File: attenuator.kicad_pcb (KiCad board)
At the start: 2 copper layers, 104.8 x 83.8 mm, 41 parts, among them J1 Conn_01x03_Male, J2 Conn_01x03_Male, J3 Conn_01x02_Male, J4 Conn_01x04_Male, J5 Conn_01x02_Male, K1 G5V-2, K2 G5V-2, K3 G5V-2, K4 G5V-2, K5 G5V-2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

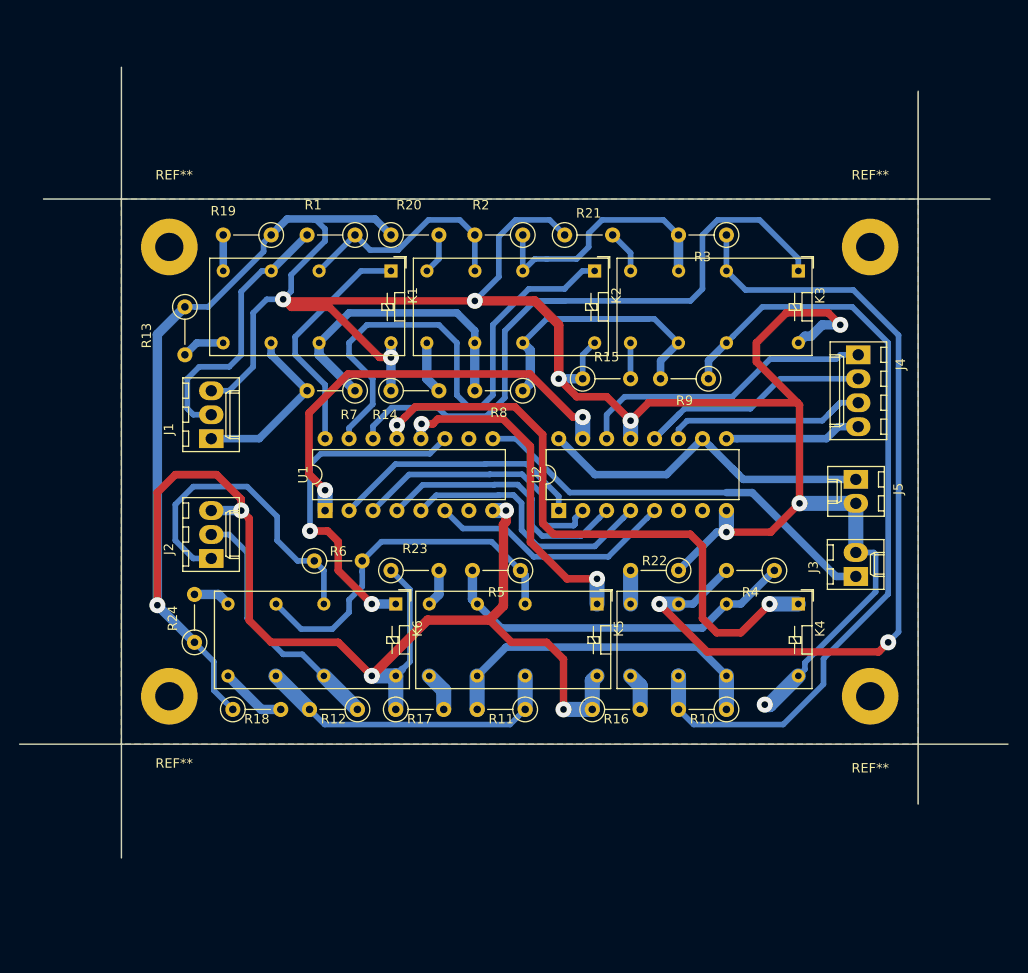
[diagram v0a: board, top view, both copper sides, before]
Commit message: change schema and working on pcb
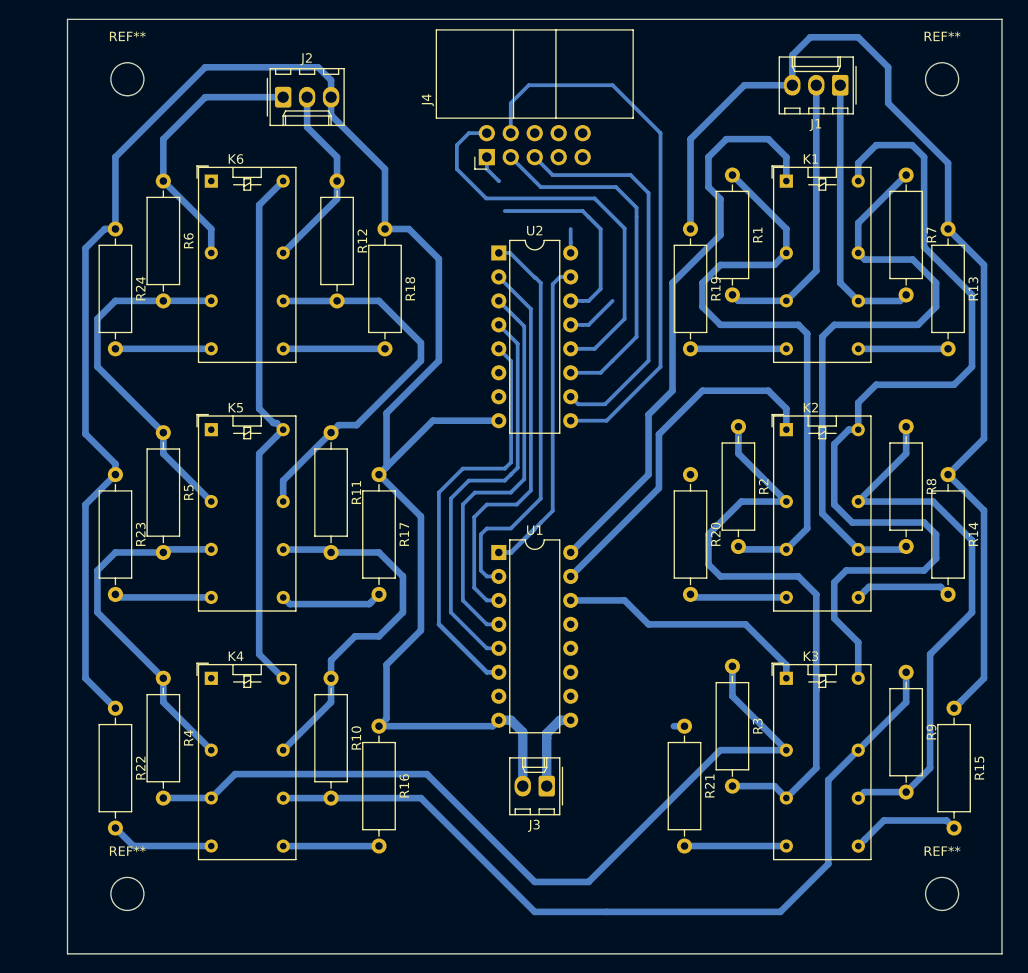
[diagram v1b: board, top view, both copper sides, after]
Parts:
- removed J5: Conn_01x02_Male, Connectors_Molex:Molex_KK-6410-02_02x2.54mm_Straight
- removed the REF** at (90.8, 54.6)
- removed the REF** at (90.8, 102.2)
- removed the REF** at (165.1, 102.2)
- removed the REF** at (165.1, 54.6)
- added REF**: MountingHole_3.5mm, MountingHole:MountingHole_3.5mm, F.Cu at (86.4, 36.8)
- added REF**: MountingHole_3.5mm, MountingHole:MountingHole_3.5mm, F.Cu at (172.7, 36.8)
- added REF**: MountingHole_3.5mm, MountingHole:MountingHole_3.5mm, F.Cu at (172.7, 123.2)
- added REF**: MountingHole_3.5mm, MountingHole:MountingHole_3.5mm, F.Cu at (86.4, 123.2)
- J1, J2: footprint Connectors_Molex:Molex_KK-6410-03_03x2.54mm_Straight -> Connector_Molex:Molex_KK-254_AE-6410-03A_1x03_P2.54mm_Vertical
- J3: footprint Connectors_Molex:Molex_KK-6410-02_02x2.54mm_Straight -> Connector_Molex:Molex_KK-254_AE-6410-02A_1x02_P2.54mm_Vertical
- J4: value Conn_01x04_Male -> Conn_01x05_Male; footprint Connectors_Molex:Molex_KK-6410-04_04x2.54mm_Straight -> Connector_IDC:IDC-Header_2x05_P2.54mm_Horizontal
- K1: footprint Relays_THT:Relay_DPDT_Omron_G5V-2 -> Relay_THT:Relay_DPDT_Omron_G5V-2
- R1, R10, R11, R12, R13, R14, R15, R16, R17, R18, R19, R2, R20, R21, R22, R23, R24, R3, R4, R5, R6, R7, R8, R9: footprint Resistors_THT:R_Axial_DIN0207_L6.3mm_D2.5mm_P5.08mm_Vertical -> Resistor_THT:R_Axial_DIN0309_L9.0mm_D3.2mm_P12.70mm_Horizontal
- U1, U2: footprint Housings_DIP:DIP-16_W7.62mm -> Package_DIP:DIP-16_W7.62mm
- moved R13 81.3 mm to (173.4, 52.7)
- moved J1 76.5 mm to (161.9, 37.5), turned to 180 degrees
- moved R4 65.8 mm to (90.2, 100.3), turned to 270 degrees
- moved R7 62.7 mm to (168.9, 47.0), turned to 270 degrees
- moved K4 62.7 mm to (95.2, 100.3), turned to 0 degrees
- moved R22 61.5 mm to (85.1, 103.5), turned to 270 degrees
- moved R14 59.7 mm to (173.4, 78.7), turned to 270 degrees
- moved R12 56.0 mm to (108.6, 47.6), turned to 270 degrees
- moved R21 53.6 mm to (145.4, 105.4), turned to 270 degrees
- moved R18 53.4 mm to (113.7, 52.7), turned to 270 degrees
- moved R15 52.6 mm to (174.0, 103.5), turned to 270 degrees
- moved J2 49.5 mm to (102.9, 38.7), turned to 0 degrees
- moved K6 48.9 mm to (95.2, 47.6), turned to 0 degrees
- moved R3 45.7 mm to (150.5, 99.1), turned to 270 degrees
- moved K5 44.9 mm to (95.2, 74.0), turned to 0 degrees
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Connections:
- K1 pad 16: GND -> +12V
- K2 pad 16: GND -> +12V
- K3 pad 16: GND -> +12V
- K4 pad 16: GND -> +12V
- K5 pad 16: GND -> +12V
- K6 pad 16: GND -> +12V
- U2 pad 10: +5V -> Net-(J4-Pad5)
- U2 pad 16: +5V -> Net-(J4-Pad5)
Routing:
- net +12V: track 45.0 -> 164.1 mm
- net GND: track 422.2 -> 332.1 mm, vias 14 -> 0
- net /K4: track 65.9 -> 0.00 mm, vias 2 -> 0
- net Net-(J4-Pad5): track 0.00 -> 44.5 mm
- net Net-(J4-Pad4): track 14.5 -> 58.6 mm
- net /K3: track 69.7 -> 27.1 mm
- net Net-(K1-Pad4): track 24.6 -> 64.6 mm
- net Net-(K2-Pad4): track 27.9 -> 65.4 mm
- net +5V: track 37.3 -> 0.00 mm
- net /K6: track 37.1 -> 0.00 mm, vias 2 -> 0
- net /K1: track 25.2 -> 61.4 mm
- net /K5: track 36.0 -> 0.00 mm, vias 2 -> 0
- net Net-(K1-Pad13): track 31.6 -> 65.2 mm
- net Net-(K2-Pad13): track 38.5 -> 58.7 mm
- net /K2: track 56.2 -> 37.4 mm
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- removed copper zone on B.Cu, net GND
- removed copper zone on F.Cu, net GND
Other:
- board size 104.8 x 83.8 mm -> 99.1 x 99.1 mm
- net class Default: clearance 0.5 -> 0.4; trace_width 0.8 -> 0.4; via_dia 1.7 -> 0.8; via_drill 0.7 -> 0.4
- rule pad_to_mask_clearance: 0.2 -> 0
- rule trace_clearance: 0.5 -> 0.4
- rule via_min_drill: 0.7 -> 0.3
- rule via_min_size: 1 -> 0.4

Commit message: Update pcb board
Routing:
- net /K5: track 0.00 -> 8.57 mm, vias 0 -> 2
- net GND: track 332.1 -> 340.5 mm, vias 0 -> 6
- net /K6: track 0.00 -> 8.25 mm, vias 0 -> 2
- net /K4: track 0.00 -> 8.25 mm, vias 0 -> 2
- net +12V: track 164.1 -> 168.6 mm, vias 0 -> 2
- net Net-(J4-Pad1): track 24.1 -> 24.5 mm, vias 0 -> 2
- net Net-(J4-Pad5): vias 0 -> 2
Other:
- net class Default: via_dia 0.8 -> 1.4; via_drill 0.4 -> 0.8
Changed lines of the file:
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@@
     (thickness 1.6)
     (drawings 4)
-    (tracks 367)
+    (tracks 413)
     (zones 0)
     (modules 40)
@@
   )
   (setup
-    (last_trace_width 0.7)
+    (last_trace_width 1)
     (user_trace_width 0.7)
     (user_trace_width 1)
@@
     (segment_width 0.2)
     (edge_width 0.1)
-    (via_size 0.8)
-    (via_drill 0.4)
+    (via_size 1.4)
+    (via_drill 0.8)
     (via_min_size 0.4)
     (via_min_drill 0.3)
@@
     (pad_drill 0.6)
     (pad_to_mask_clearance 0)
+    (solder_mask_min_width 0.25)
     (aux_axis_origin 0 0)
-    (visible_elements FFFFFF7F)
+    (visible_elements 7FFFFFFF)
     (pcbplotparams
       (layerselection 0x010fc_ffffffff)
@@
     (clearance 0.4)
     (trace_width 0.4)
-    (via_dia 0.8)
-    (via_drill 0.4)
+    (via_dia 1.4)
+    (via_drill 0.8)
     (uvia_dia 0.3)
     (uvia_drill 0.1)
@@
   (segment (start 125.095 105.41) (end 125.73 104.775) (width 0.7) (layer B.Cu) (net 3))
   (segment (start 113.03 105.41) (end 125.095 105.41) (width 0.7) (layer B.Cu) (net 3))
-  (segment (start 133.35 62.865) (end 134.62 62.865) (width 0.4) (layer B.Cu) (net 3))
-  (segment (start 134.62 62.865) (end 135.255 62.865) (width 0.4) (layer B.Cu) (net 3))
-  (segment (start 135.255 62.865) (end 137.795 60.325) (width 0.4) (layer B.Cu) (net 3))
   (segment (start 118.745 73.025) (end 113.03 78.74) (width 0.7) (layer B.Cu) (net 3))
-  (segment (start 125.73 73.025) (end 118.745 73.025) (width 0.7) (layer B.Cu) (net 3))
+  (segment (start 125.73 73.025) (end 121.92 73.025) (width 0.7) (layer B.Cu) (net 3))
   (segment (start 113.829999 104.610001) (end 113.829999 98.895001) (width 0.7) (layer B.Cu) (net 3))
   (segment (start 113.03 105.41) (end 113.829999 104.610001) (width 0.7) (layer B.Cu) (net 3))
@@
   (segment (start 117.475 83.185) (end 113.03 78.74) (width 0.7) (layer B.Cu) (net 3))
   (segment (start 117.475 95.25) (end 117.475 83.185) (width 0.7) (layer B.Cu) (net 3))
+  (segment (start 137.795 60.325) (end 137.795 60.325) (width 0.4) (layer B.Cu) (net 3))
+  (via (at 137.795 60.325) (size 1.4) (drill 0.8) (layers F.Cu B.Cu) (net 3))
+  (segment (start 146.05 78.74) (end 146.05 75.565) (width 1) (layer B.Cu) (net 3))
+  (segment (start 146.05 75.565) (end 146.05 75.565) (width 1) (layer B.Cu) (net 3))
+  (via (at 146.05 75.565) (size 1.4) (drill 0.8) (layers F.Cu B.Cu) (net 3))
+  (via (at 135.89 62.23) (size 1.4) (drill 0.8) (layers F.Cu B.Cu) (net 3))
+  (segment (start 135.255 62.865) (end 135.89 62.23) (width 1) (layer B.Cu) (net 3))
+  (segment (start 133.35 62.865) (end 135.255 62.865) (width 1) (layer B.Cu) (net 3))
+  (segment (start 137.795 60.325) (end 135.89 62.23) (width 1) (layer B.Cu) (net 3))
+  (segment (start 145.250001 53.504999) (end 145.250001 54.774999) (width 1) (layer B.Cu) (net 3))
+  (segment (start 146.05 52.705) (end 145.250001 53.504999) (width 1) (layer B.Cu) (net 3))
+  (segment (start 145.250001 54.774999) (end 145.250001 54.774999) (width 1) (layer B.Cu) (net 3))
+  (via (at 145.250001 54.774999) (size 1.4) (drill 0.8) (layers F.Cu B.Cu) (net 3))
+  (segment (start 121.92 73.025) (end 118.745 73.025) (width 0.7) (layer B.Cu) (net 3))
+  (via (at 121.92 73.025) (size 1.4) (drill 0.8) (layers F.Cu B.Cu) (net 3))
+  (segment (start 146.749999 74.865001) (end 147.32 73.025) (width 1) (layer B.Cu) (net 3))
+  (segment (start 146.05 75.565) (end 146.749999 74.865001) (width 1) (layer B.Cu) (net 3))
+  (via (at 147.32 73.025) (size 1.4) (drill 0.8) (layers F.Cu B.Cu) (net 3))
   (segment (start 108.585 49.53) (end 108.585 47.625) (width 0.7) (layer B.Cu) (net 4))
   (segment (start 102.87 55.245) (end 108.585 49.53) (width 0.7) (layer B.Cu) (net 4))
@@
   (segment (start 169.545 43.815) (end 165.735 43.815) (width 0.7) (layer B.Cu) (net 6))
   (segment (start 163.83 45.72) (end 163.83 47.625) (width 0.7) (layer B.Cu) (net 6))
-  (segment (start 163.83 100.33) (end 163.83 96.52) (width 0.7) (layer B.Cu) (net 6))
+  (segment (start 163.83 100.33) (end 163.83 97.155) (width 0.7) (layer B.Cu) (net 6))
   (segment (start 163.83 96.52) (end 161.29 93.98) (width 0.7) (layer B.Cu) (net 6))
   (segment (start 161.29 93.98) (end 161.29 90.17) (width 0.7) (layer B.Cu) (net 6))
@@
   (segment (start 100.33 71.755) (end 100.33 50.165) (width 0.7) (layer B.Cu) (net 6))
   (segment (start 100.33 50.165) (end 102.87 47.625) (width 0.7) (layer B.Cu) (net 6))
+  (segment (start 133.35 104.775) (end 137.795 104.775) (width 1) (layer B.Cu) (net 6))
+  (segment (start 137.795 104.775) (end 137.795 104.775) (width 1) (layer B.Cu) (net 6))
+  (via (at 137.795 104.775) (size 1.4) (drill 0.8) (layers F.Cu B.Cu) (net 6))
+  (segment (start 163.83 97.155) (end 163.83 96.52) (width 0.7) (layer B.Cu) (net 6))
+  (via (at 163.83 97.155) (size 1.4) (drill 0.8) (layers F.Cu B.Cu) (net 6))
   (segment (start 133.35 60.325) (end 134.62 60.325) (width 0.4) (layer B.Cu) (net 7))
   (segment (start 134.62 60.325) (end 135.255 60.325) (width 0.4) (layer B.Cu) (net 7))
   (segment (start 135.255 60.325) (end 136.525 59.055) (width 0.4) (layer B.Cu) (net 7))
   (segment (start 136.525 59.055) (end 136.525 52.705) (width 0.4) (layer B.Cu) (net 7))
-  (segment (start 124.46 46.3486) (end 125.73 47.6186) (width 0.4) (layer B.Cu) (net 7))
+  (segment (start 124.46 46.3486) (end 126.3586 47.6186) (width 0.4) (layer B.Cu) (net 7))
   (segment (start 124.46 45.085) (end 124.46 46.3486) (width 0.4) (layer B.Cu) (net 7))
-  (segment (start 125.73 47.6186) (end 125.73 47.625) (width 0.4) (layer B.Cu) (net 7))
   (segment (start 136.525 52.705) (end 135.255 51.435) (width 0.4) (layer B.Cu) (net 7))
   (segment (start 135.255 51.435) (end 134.62 50.8) (width 0.4) (layer B.Cu) (net 7))
   (segment (start 134.62 50.8) (end 126.365 50.8) (width 0.4) (layer B.Cu) (net 7))
+  (segment (start 126.365 50.8) (end 126.365 50.8) (width 0.4) (layer B.Cu) (net 7))
+  (via (at 126.365 50.8) (size 1.4) (drill 0.8) (layers F.Cu B.Cu) (net 7))
+  (via (at 126.3586 47.6186) (size 1.4) (drill 0.8) (layers F.Cu B.Cu) (net 7))
   (segment (start 122.555 42.545) (end 124.46 42.545) (width 0.4) (layer B.Cu) (net 8))
   (segment (start 121.285 43.815) (end 122.555 42.545) (width 0.4) (layer B.Cu) (net 8))
@@
   (segment (start 133.35 70.485) (end 134.149999 71.284999) (width 0.4) (layer B.Cu) (net 11))
   (segment (start 136.995001 71.284999) (end 141.605 66.675) (width 0.4) (layer B.Cu) (net 11))
-  (segment (start 141.605 66.675) (end 141.605 48.895) (width 0.4) (layer B.Cu) (net 11))
+  (segment (start 141.605 66.675) (end 141.605 52.705) (width 0.4) (layer B.Cu) (net 11))
   (segment (start 134.149999 71.284999) (end 136.995001 71.284999) (width 0.4) (layer B.Cu) (net 11))
   (segment (start 141.605 48.895) (end 139.7 46.99) (width 0.4) (layer B.Cu) (net 11))
@@
   (segment (start 133.35 55.245) (end 133.35 54.11363) (width 0.4) (layer B.Cu) (net 11))
   (segment (start 133.35 54.11363) (end 133.35 52.705) (width 0.4) (layer B.Cu) (net 11))
+  (segment (start 133.35 52.705) (end 133.35 52.705) (width 0.4) (layer B.Cu) (net 11))
+  (via (at 133.35 52.705) (size 1.4) (drill 0.8) (layers F.Cu B.Cu) (net 11))
+  (segment (start 141.605 52.705) (end 141.605 48.895) (width 0.4) (layer B.Cu) (net 11))
+  (via (at 141.605 52.705) (size 1.4) (drill 0.8) (layers F.Cu B.Cu) (net 11))
   (segment (start 163.83 52.07) (end 168.91 46.99) (width 0.7) (layer B.Cu) (net 12))
   (segment (start 163.83 55.245) (end 163.83 52.07) (width 0.7) (layer B.Cu) (net 12))
@@
   (segment (start 86.995 118.11) (end 85.09 116.205) (width 0.7) (layer B.Cu) (net 30))
   (segment (start 95.25 118.11) (end 86.995 118.11) (width 0.7) (layer B.Cu) (net 30))
+  (segment (start 133.35 94.615) (end 137.795 94.615) (width 1) (layer B.Cu) (net 31))
+  (segment (start 137.795 94.615) (end 137.795 94.615) (width 1) (layer B.Cu) (net 31))
+  (via (at 137.795 94.615) (size 1.4) (drill 0.8) (layers F.Cu B.Cu) (net 31))
+  (segment (start 95.25 100.33) (end 95.25 98.63) (width 1) (layer B.Cu) (net 31))
+  (segment (start 95.25 98.63) (end 95.25 96.52) (width 1) (layer B.Cu) (net 31))
+  (segment (start 95.25 96.52) (end 95.25 96.52) (width 1) (layer B.Cu) (net 31))
+  (via (at 95.25 96.52) (size 1.4) (drill 0.8) (layers F.Cu B.Cu) (net 31))
+  (segment (start 133.35 97.155) (end 137.795 97.155) (width 1) (layer B.Cu) (net 32))
+  (segment (start 137.795 97.155) (end 137.795 97.155) (width 1) (layer B.Cu) (net 32))
+  (via (at 137.795 97.155) (size 1.4) (drill 0.8) (layers F.Cu B.Cu) (net 32))
+  (segment (start 95.25 73.9775) (end 95.25 72.2775) (width 1) (layer B.Cu) (net 32))
+  (segment (start 95.25 72.2775) (end 95.25 69.85) (width 1) (layer B.Cu) (net 32))
+  (segment (start 95.25 69.85) (end 95.25 69.85) (width 1) (layer B.Cu) (net 32))
+  (via (at 95.25 69.85) (size 1.4) (drill 0.8) (layers F.Cu B.Cu) (net 32))
   (segment (start 85.4075 91.7575) (end 85.09 91.44) (width 0.7) (layer B.Cu) (net 33))
   (segment (start 95.25 91.7575) (end 85.4075 91.7575) (width 0.7) (layer B.Cu) (net 33))
@@
   (segment (start 113.665 65.405) (end 102.89 65.405) (width 0.7) (layer B.Cu) (net 37))
   (segment (start 85.09 65.405) (end 95.25 65.405) (width 0.7) (layer B.Cu) (net 38))
+  (segment (start 133.35 99.695) (end 137.795 99.695) (width 1) (layer B.Cu) (net 39))
+  (segment (start 137.795 99.695) (end 137.795 99.695) (width 1) (layer B.Cu) (net 39))
+  (via (at 137.795 99.695) (size 1.4) (drill 0.8) (layers F.Cu B.Cu) (net 39))
+  (segment (start 95.25 47.625) (end 95.25 43.815) (width 1) (layer B.Cu) (net 39))
+  (segment (start 95.25 43.815) (end 95.25 43.815) (width 1) (layer B.Cu) (net 39))
+  (via (at 95.25 43.815) (size 1.4) (drill 0.8) (layers F.Cu B.Cu) (net 39))
   (segment (start 125.73 99.695) (end 124.46 99.695) (width 0.5) (layer B.Cu) (net 41))
   (segment (start 127.030001 66.705001) (end 127.030001 77.439999) (width 0.4) (layer B.Cu) (net 41))

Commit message: First version of pcb booard
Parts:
- R20: footprint Resistor_THT:R_Axial_DIN0309_L9.0mm_D3.2mm_P12.70mm_Horizontal -> Resistor_THT:R_Axial_DIN0309_L9.0mm_D3.2mm_P20.32mm_Horizontal
- moved R20 18.2 mm to (137.2, 62.9)
- moved R21 16.3 mm to (129.5, 109.2), turned to 0 degrees
- moved J3 4.02 mm to (132.1, 115.6)
- moved R3 2.62 mm to (149.9, 101.6)
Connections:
- J4 pad 7: (no net) -> Net-(J4-Pad5)
- J4 pad 9: (no net) -> Net-(J4-Pad5)
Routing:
- net +12V: track 168.6 -> 297.2 mm, vias 2 -> 1
- net /K6: track 8.25 -> 124.7 mm
- net GND: track 340.5 -> 420.5 mm, vias 6 -> 2
- net /K5: track 8.57 -> 78.4 mm
- net /K4: track 8.25 -> 65.7 mm
- net Net-(J4-Pad5): track 44.5 -> 80.5 mm
- net Net-(K2-Pad8): track 10.3 -> 24.1 mm
- net Net-(K3-Pad8): track 10.8 -> 19.9 mm
- net Net-(J4-Pad1): track 24.5 -> 30.2 mm, vias 2 -> 0
- net Net-(K3-Pad4): track 88.9 -> 94.0 mm
- net Net-(K5-Pad4): track 37.2 -> 42.3 mm
- net Net-(K4-Pad13): track 39.0 -> 35.8 mm
- net /K2: track 37.4 -> 40.3 mm
- net /K1: track 61.4 -> 63.9 mm
- net Net-(J4-Pad2): track 43.2 -> 45.1 mm, vias 0 -> 2
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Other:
- net class Default: via_dia 1.4 -> 1.8
